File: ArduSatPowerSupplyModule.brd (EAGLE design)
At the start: 95.5 x 90.3 mm, 168 parts, among them IC1 AVR-MEGA8-MI, IC10 TMP102, IC11 TMP102, IC2 ATMEGA16U2-MU, IC3 LTC3115, IC4 LTC4078, IC5 MAX17043G+U, IC6 MAX4372F, IC7 LTC3536, IC8 MAX4372F, IC9 LTC3536, Q1 RJU003N03 N-MOSFET, Q2 RJU003N03 N-MOSFET, Q3 MOSFET-PCHANNELSMT2, Q4 RJU003N03 N-MOSFET, Q5 RJU003N03 N-MOSFET, Q6 RJU003N03 N-MOSFET, Q7 RJU003N03 N-MOSFET, Q8 RJU003N03 N-MOSFET, Q9 RJU003N03 N-MOSFET, SW1 RESET, SW2 SWITCH-SPDT

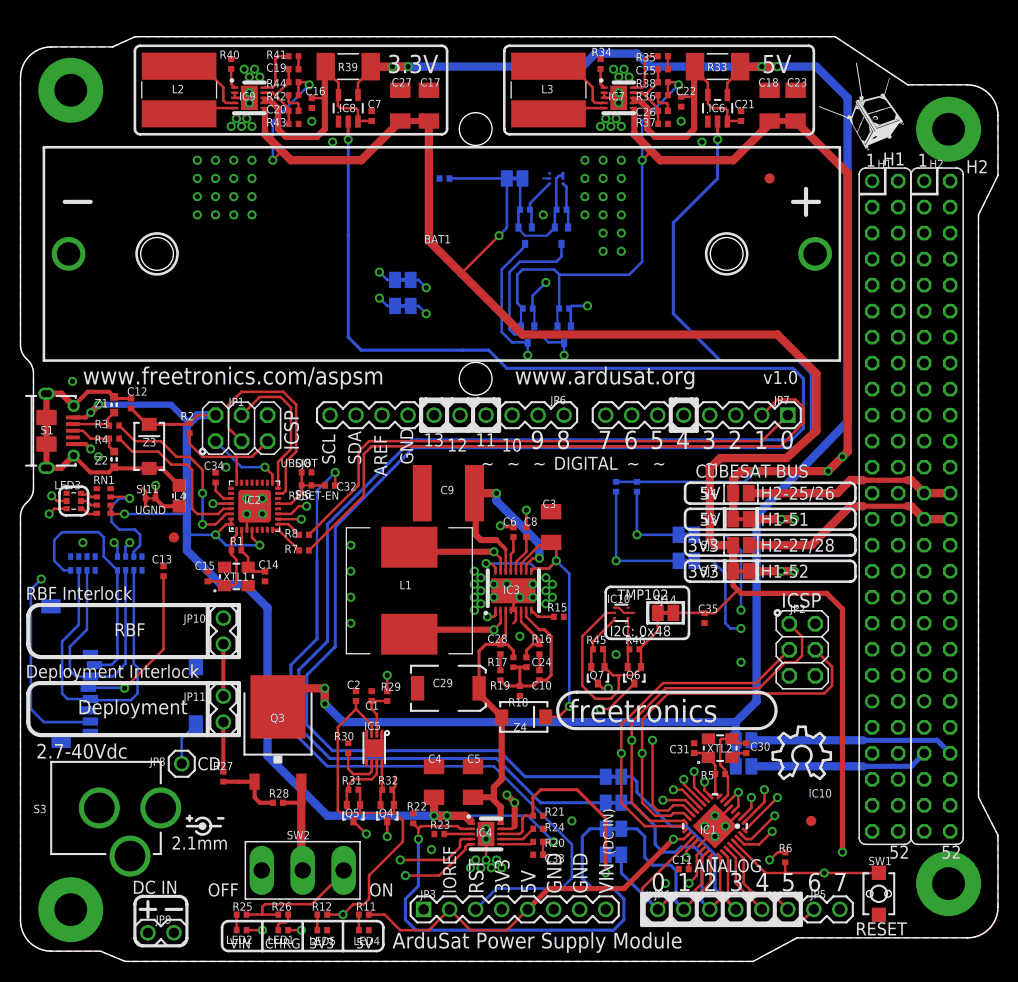
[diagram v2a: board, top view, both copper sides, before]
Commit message: Changed max charge rate to 1A; removed solder jumpers for ArduSat power pins
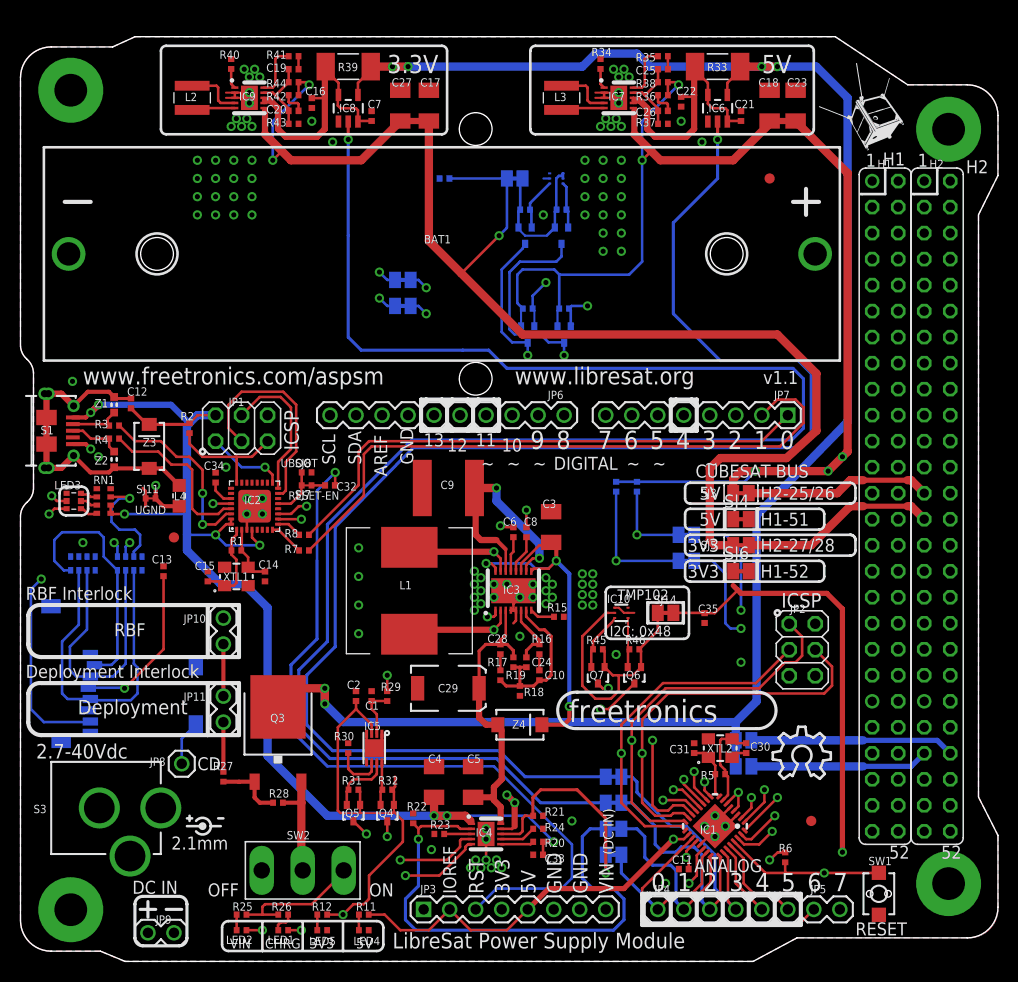
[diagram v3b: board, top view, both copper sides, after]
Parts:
- C12, C34: value 1uF 0603 -> 1uF 0402
- IC1: value AVR-MEGA8-MI -> ATmega328P
- L2, L3: value 4.7uH -> 4.7uH Coilcraft XFL4020; device freetronics-luke:CDRH -> freetronics-jon:XFL4020
- L4: device freetronics-master-v1:0805-LARGE -> freetronics-master-v1.1:0805-LARGE
- R21: value 1.05K 1% 0603 -> 1K 1% 0402
- R22: value 1.18K 1% 0603 -> 1K 1% 0402
- R24: value 10K 0603 -> 10K 0402
- SJ4: value 5V_EN -> SJCN; device freetronics-master-v1.1:SJ -> freetronics-jon:SJC
- SJ5: device freetronics-master-v1.1:SJ -> freetronics-jon:SJC
- SJ6: value RESET-EN -> SJCN; device freetronics-jon:0402SJC -> freetronics-jon:SJC
- SJ7: value 3V3_EN -> RESET-EN; device freetronics-jon:SJC -> freetronics-jon:0402SJC
- moved SJ6 43.2 mm to (70.4, 38.1)
- moved SJ7 43.2 mm to (27.9, 46.5)
- moved SJ3 2.54 mm to (70.4, 45.7)
- moved SJ4 2.54 mm to (70.4, 43.2)
- moved L3 1.48 mm to (52.8, 84.3)
- moved L2 1.48 mm to (16.8, 84.3)
- moved Z4 0.85 mm to (48.8, 23.1)
- moved C9 0.51 mm to (41.8, 46.2)
- renumbered U$10 to FID1, U$28 to FID2, U$29 to FID3
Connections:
- net D2_SDA renamed D2
- net D3_SCL renamed D3
- removed net +3V3_AS: H1.52, SJ7.2
- removed net +5V_AS: H1.51, SJ3.2
- removed net +5V_SYS: H2.25, H2.26, SJ4.2
- removed net VCC_SYS: H2.27, H2.28, SJ5.2
- new net +5V_SYS_25: H2.25, SJ3.2
- new net +5V_SYS_26: H2.26, SJ4.2
- new net H1_51: H1.51
- new net H1_52: H1.52
- new net VCC_SYS_27: H2.27, SJ5.2
- new net VCC_SYS_28: H2.28, SJ6.2
- net 3.3V: now also SJ6.1; no longer SJ7.1
- net DTR: now also SJ7.1; no longer SJ6.1
- net N$60: now also SJ7.2; no longer SJ6.2
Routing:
- net +5V_AS: track 52.3 -> 0.00 mm, vias 2 -> 0
- net +3V3_AS: track 39.5 -> 0.00 mm, vias 2 -> 0
- net VCC_SYS: track 21.8 -> 0.00 mm
- net +5V_SYS: track 20.7 -> 0.00 mm
- net VCC_SYS_27: track 0.00 -> 19.2 mm
- net +5V_SYS_25: track 0.00 -> 18.2 mm
- net GND: track 31.1 -> 36.7 mm, vias 107 -> 115
- net 3.3V: track 349.1 -> 345.1 mm
- net 5V: track 234.8 -> 232.3 mm
- net N$22: track 7.76 -> 5.60 mm
- net N$18: track 7.66 -> 5.60 mm
- net PVIN: track 127.9 -> 129.3 mm
- net N$39: track 35.8 -> 37.2 mm
- net N$19: track 5.67 -> 4.24 mm
- net N$28: track 5.61 -> 4.24 mm
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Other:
- board text added: "LibreSat Power Supply Module"
- board text added: "SKU: LSPSM"
- board text added: "v1.1"
- board text added: "www.libresat.org"
- board text removed: "ArduSat Power Supply Module"
- board text removed: "IC10"
- board text removed: "SKU: ASPSM"
